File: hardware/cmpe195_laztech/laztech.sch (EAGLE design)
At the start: 7 parts

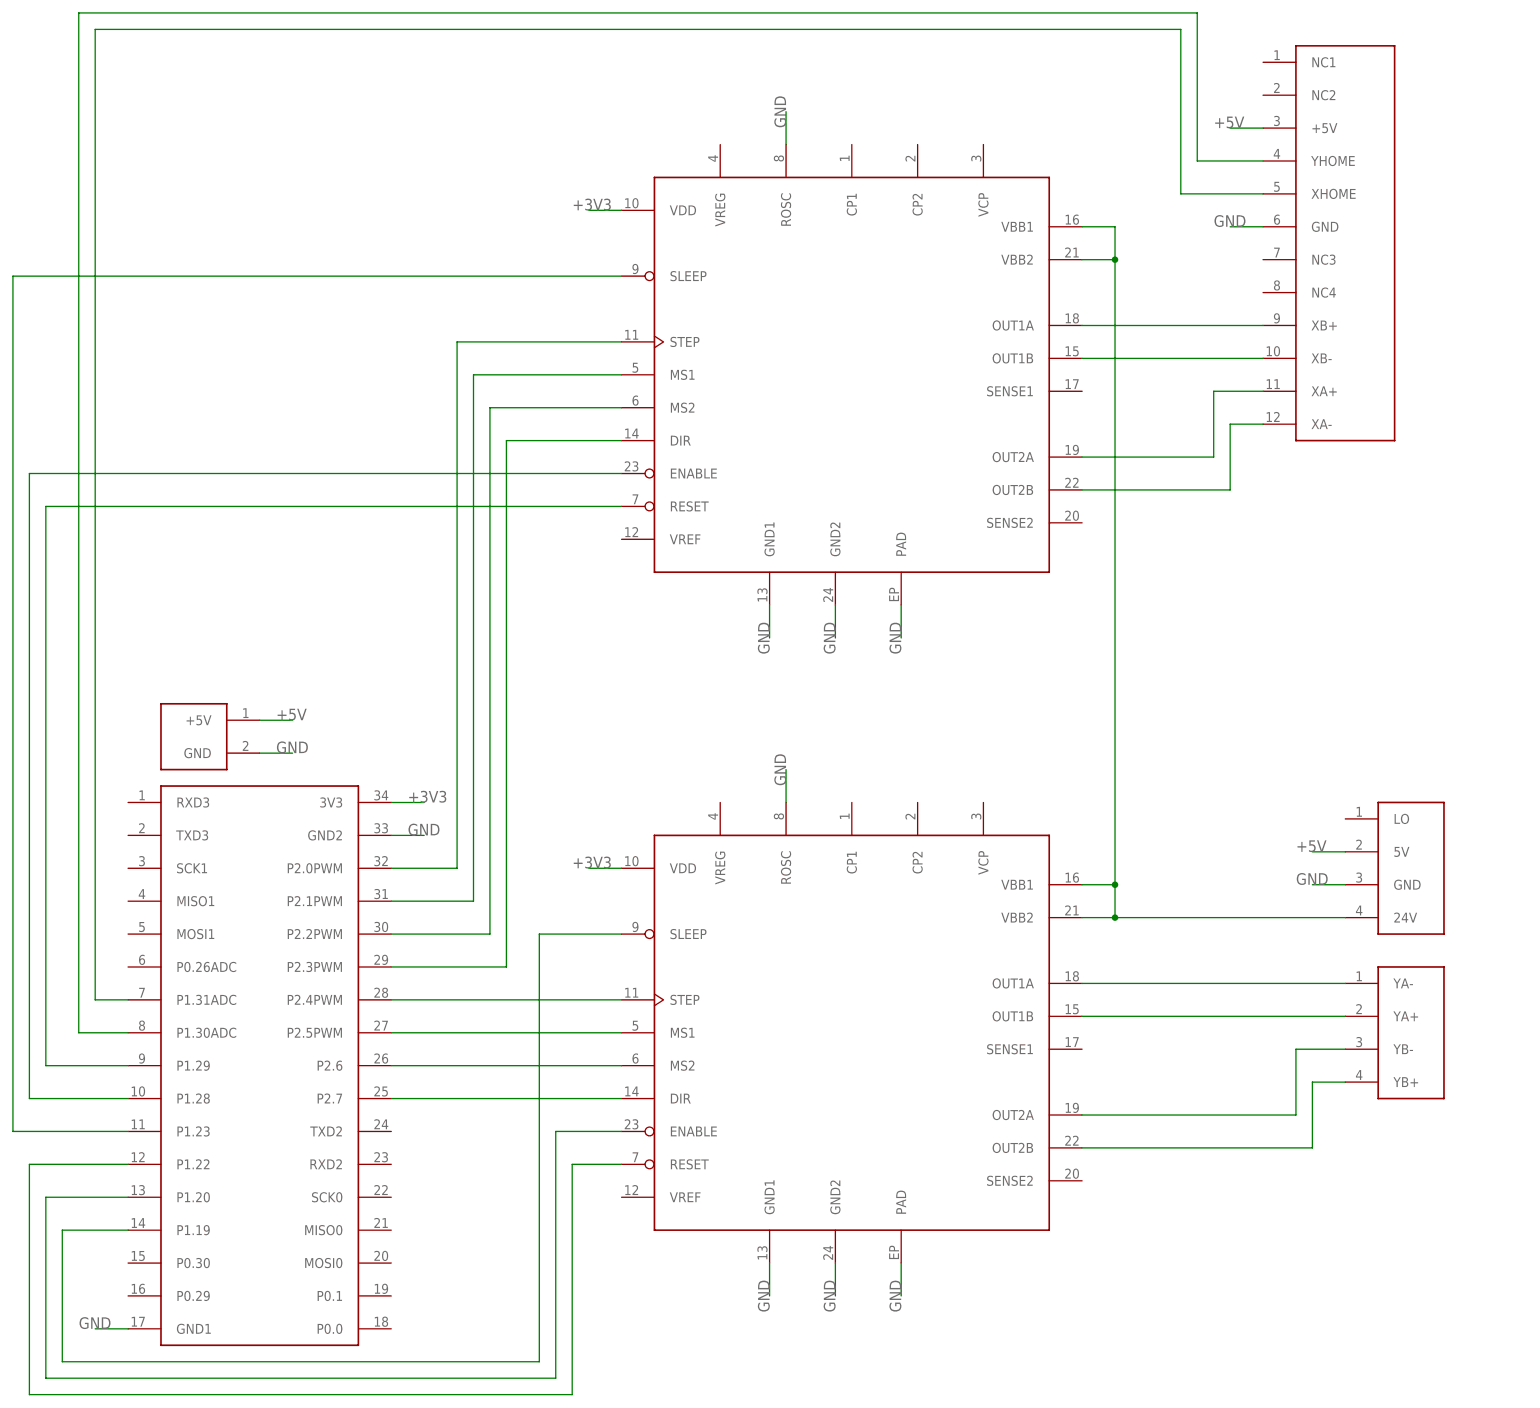
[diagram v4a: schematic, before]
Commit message: Added capacitors to sch and brd.
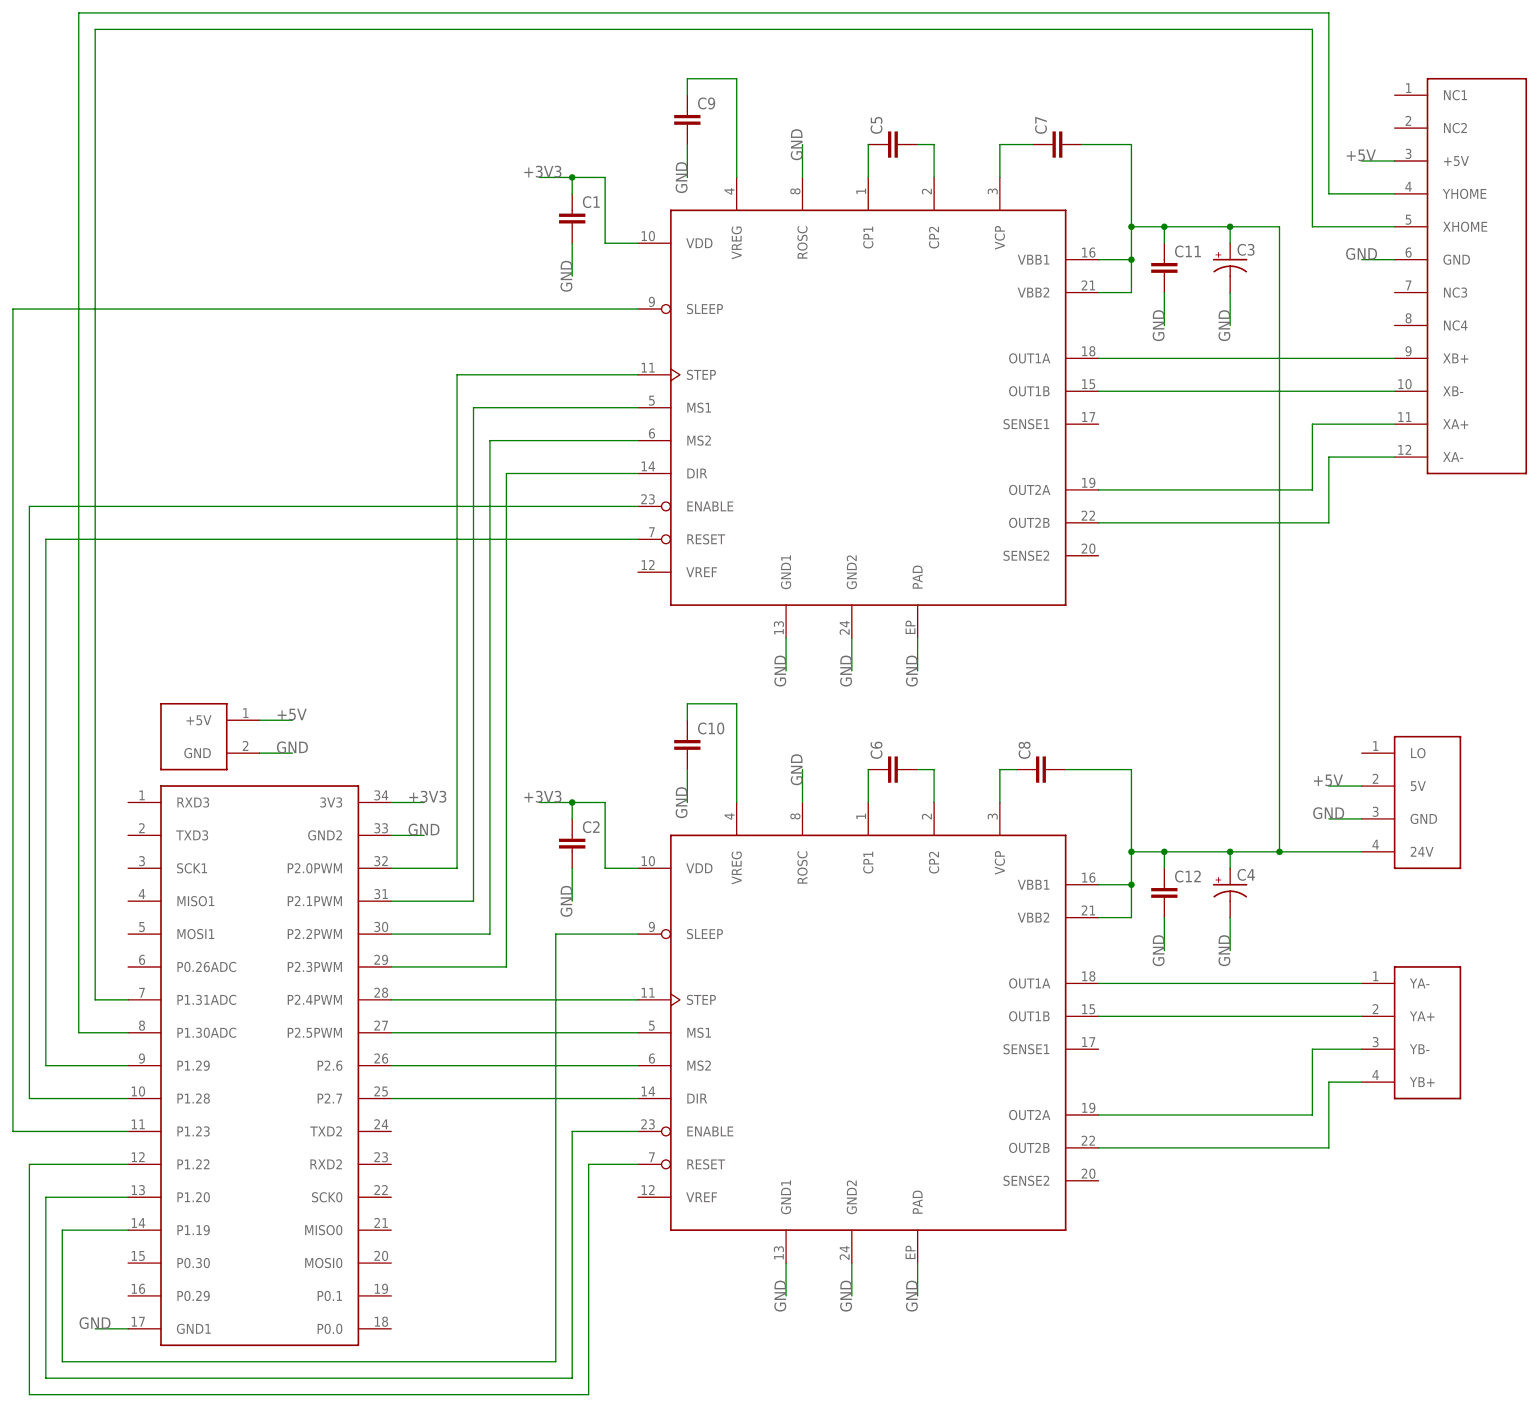
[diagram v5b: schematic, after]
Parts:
- added C1, C10, C11, C12, C2, C5, C6, C7, C8, C9: (no value), laztech_parts:CAP
- added C3, C4: (no value), laztech_parts:PCAP
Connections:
- new net N$26: C10.1, U$2.VREG
- new net N$27: C6.1, U$2.CP1
- new net N$28: C6.2, U$2.CP2
- new net N$29: C8.1, U$2.VCP
- new net N$30: C9.1, U$1.VREG
- new net N$31: C5.1, U$1.CP1
- new net N$32: C5.2, U$1.CP2
- new net N$33: C7.1, U$1.VCP
- net +3V3: now also C1.1, C2.1
- net GND: now also C1.2, C10.2, C11.2, C12.2, C2.2, C3.-, C4.-, C9.2
- net N$9: now also C11.1, C12.1, C3.+, C4.+, C7.2, C8.2

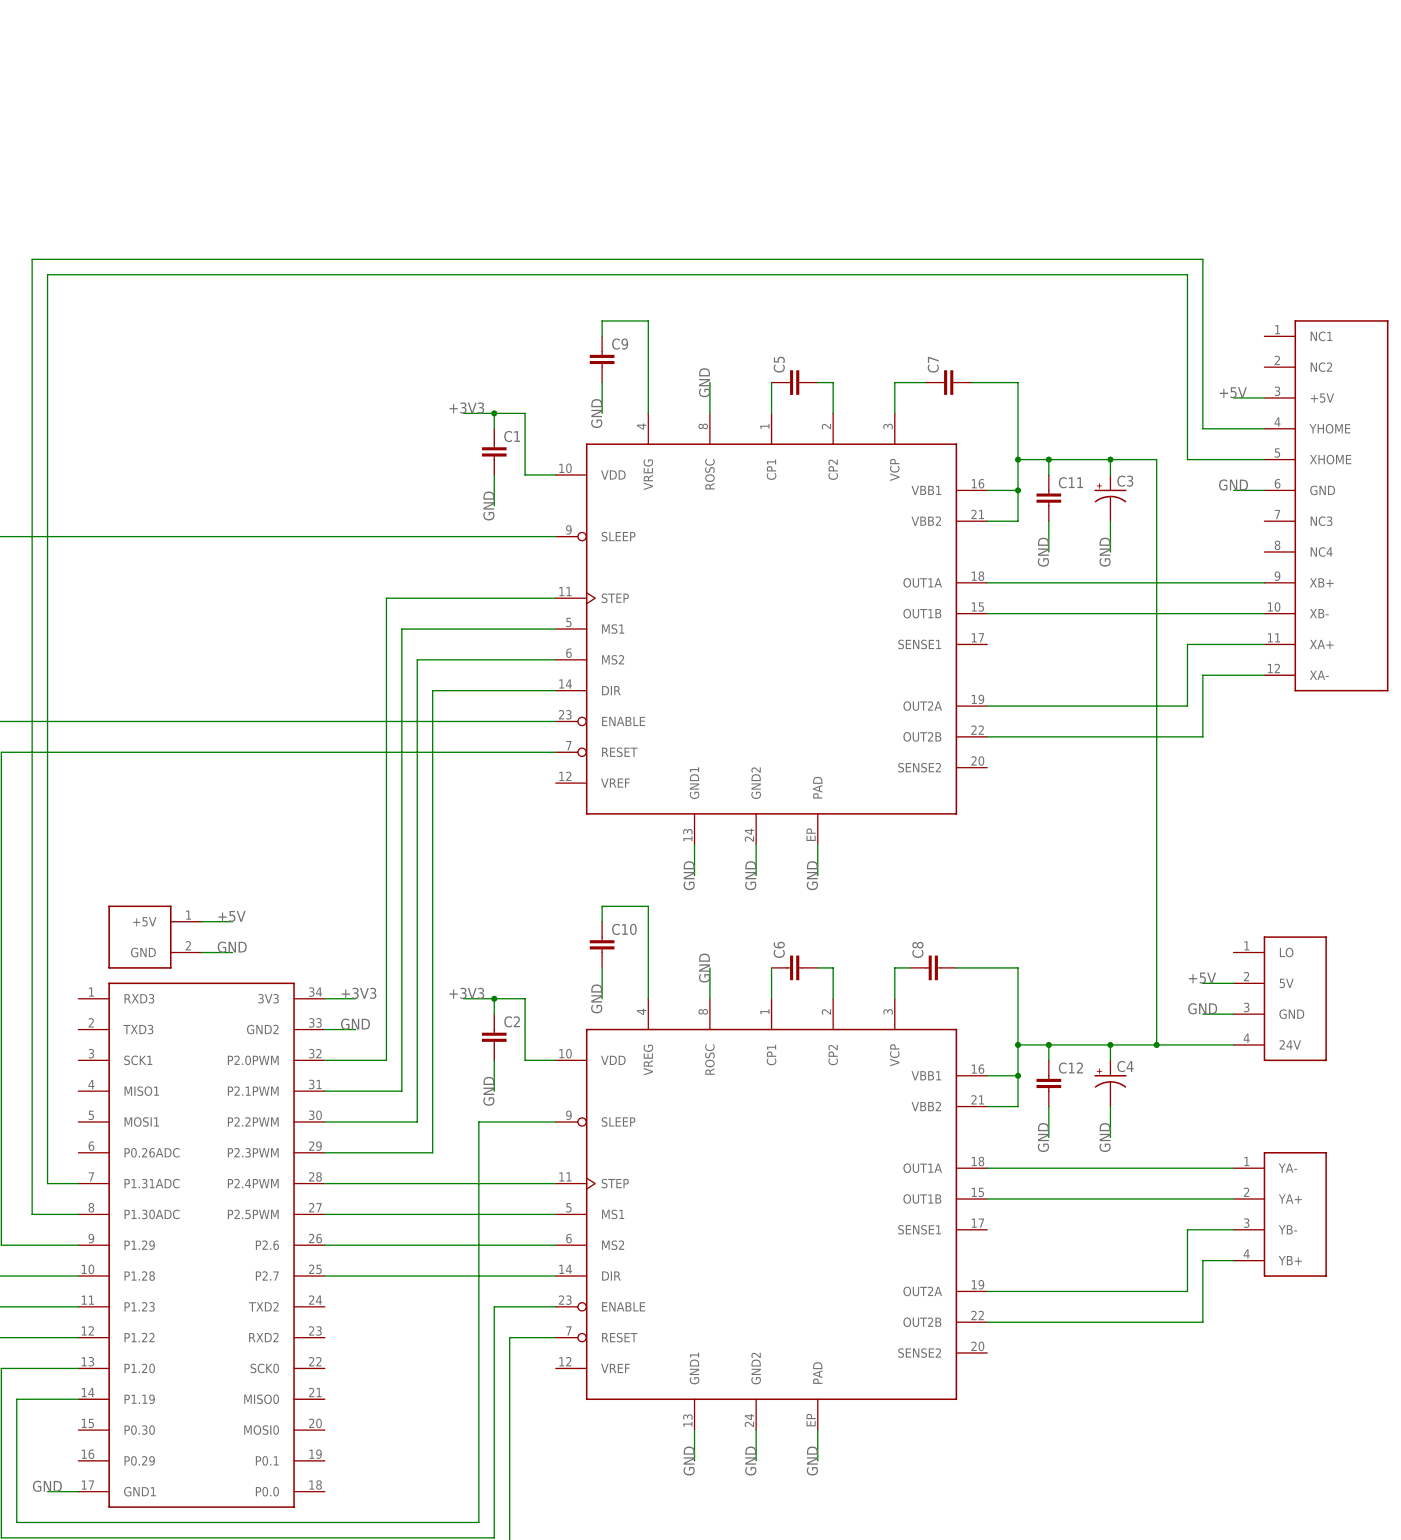
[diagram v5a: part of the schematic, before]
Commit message: Added LM317.
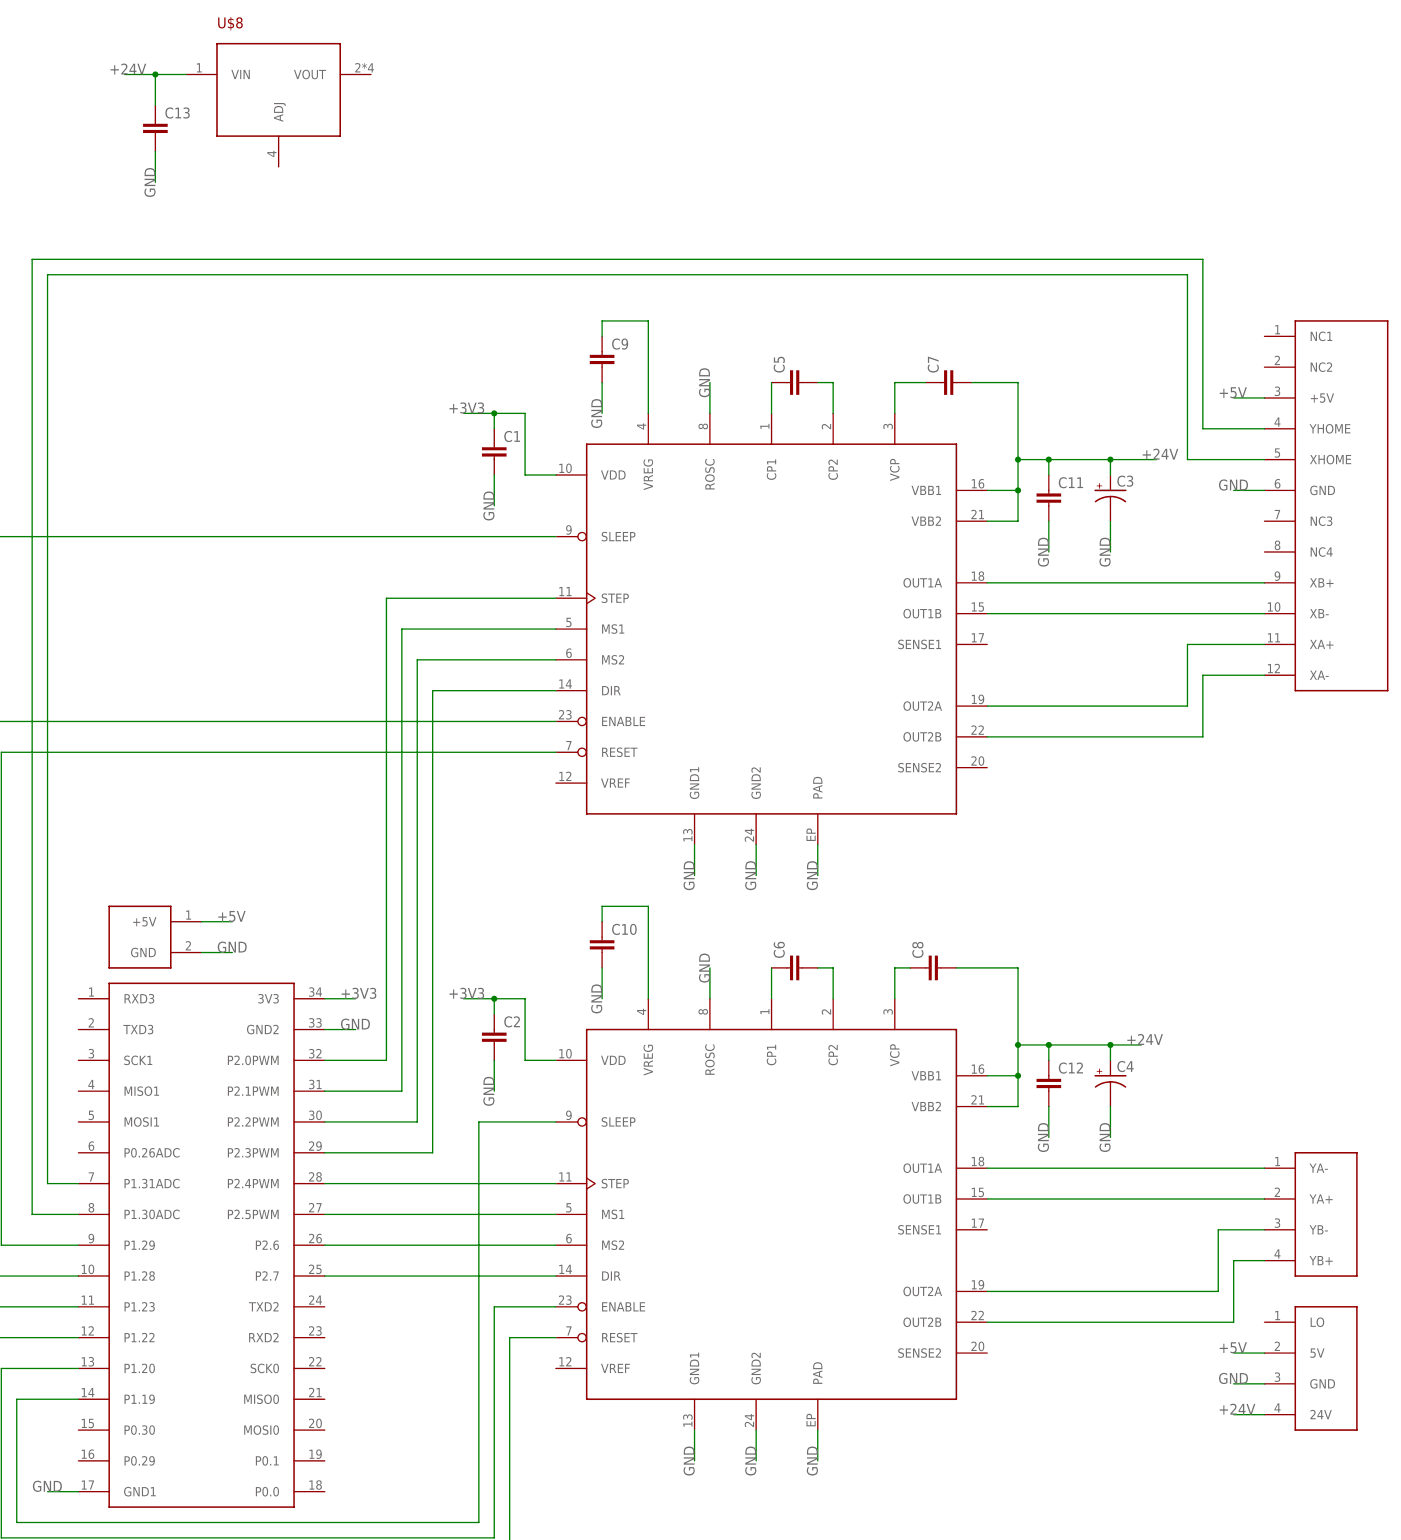
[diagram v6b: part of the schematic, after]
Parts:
- added C13: (no value), laztech_parts:CAP
- added U$8: LM317, laztech_parts:LM317
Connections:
- removed net N$9: C11.1, C12.1, C3.+, C4.+, C7.2, C8.2, U$1.VBB1, U$1.VBB2, U$2.VBB1, U$2.VBB2, U$4.24V
- new net +24V: C11.1, C12.1, C13.1, C3.+, C4.+, C7.2, C8.2, U$1.VBB1, U$1.VBB2, U$2.VBB1, U$2.VBB2, U$4.24V, U$8.VIN
- net GND: now also C13.2

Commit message: Added pin directions and resistor symbols.
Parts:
- added R1, R2, R3, R4, R5, R6, R7: RES, laztech_parts:RES
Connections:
- new net N$34: R2.1, R3.2, U$8.VOUT
- new net N$35: R5.1, U$1.SENSE2
- new net N$38: R6.1, U$2.SENSE1
- new net N$40: R7.1, U$2.SENSE2
- new net N$9: R4.1, U$1.SENSE1
- new net VREF: R1.2, R2.2, R3.1, U$1.VREF, U$2.VREF, U$8.ADJ
- net +24V: now also U$4.+24V; no longer U$4.24V
- net +5V: now also U$4.+5V; no longer U$4.5V
- net GND: now also R1.1, R4.2, R5.2, R6.2, R7.2
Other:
- moved on the sheet: C1, C10, C11, C12, C13, C2, C3, C4, C5, C6, C7, C8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
